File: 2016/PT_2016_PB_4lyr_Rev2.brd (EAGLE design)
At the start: 154.7 x 201.9 mm, 156 parts, among them Q12 2N7002, Q2 2N7002

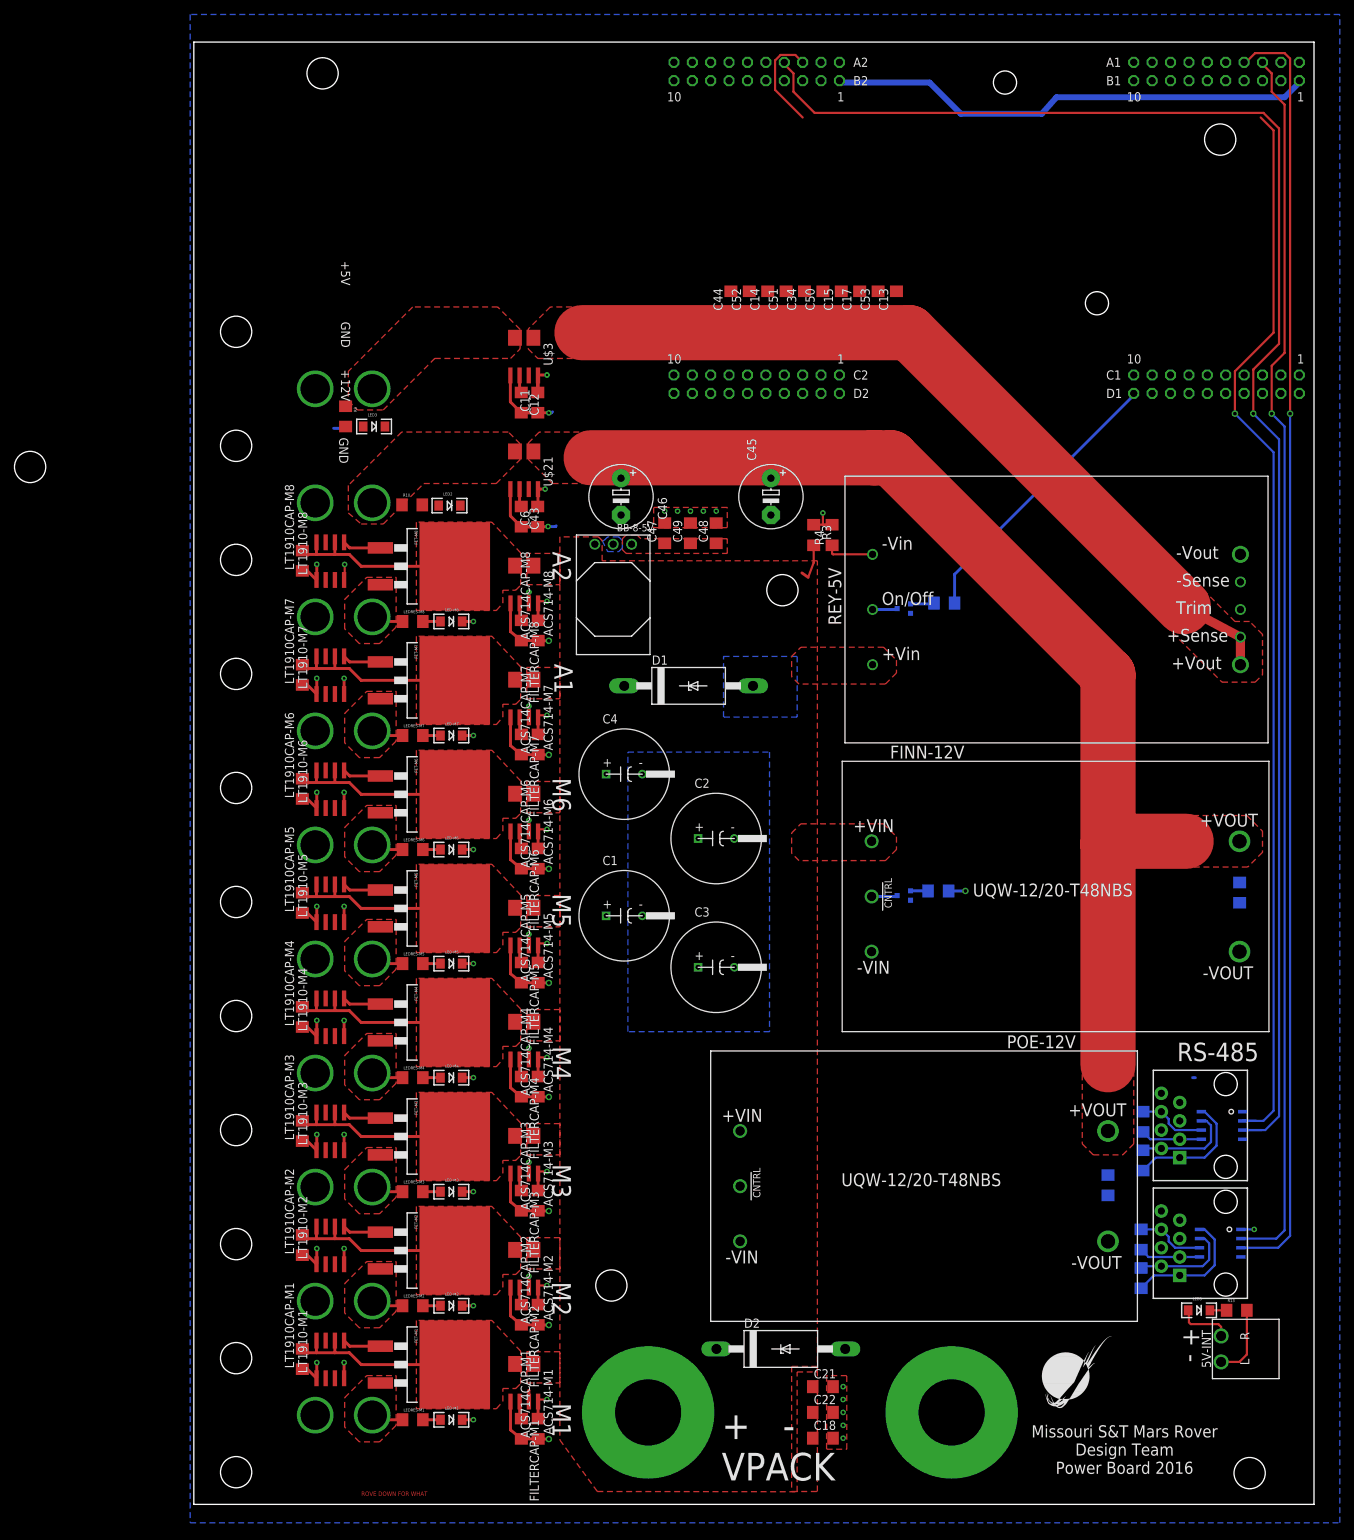
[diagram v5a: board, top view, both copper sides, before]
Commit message: Finished routing 4-layer
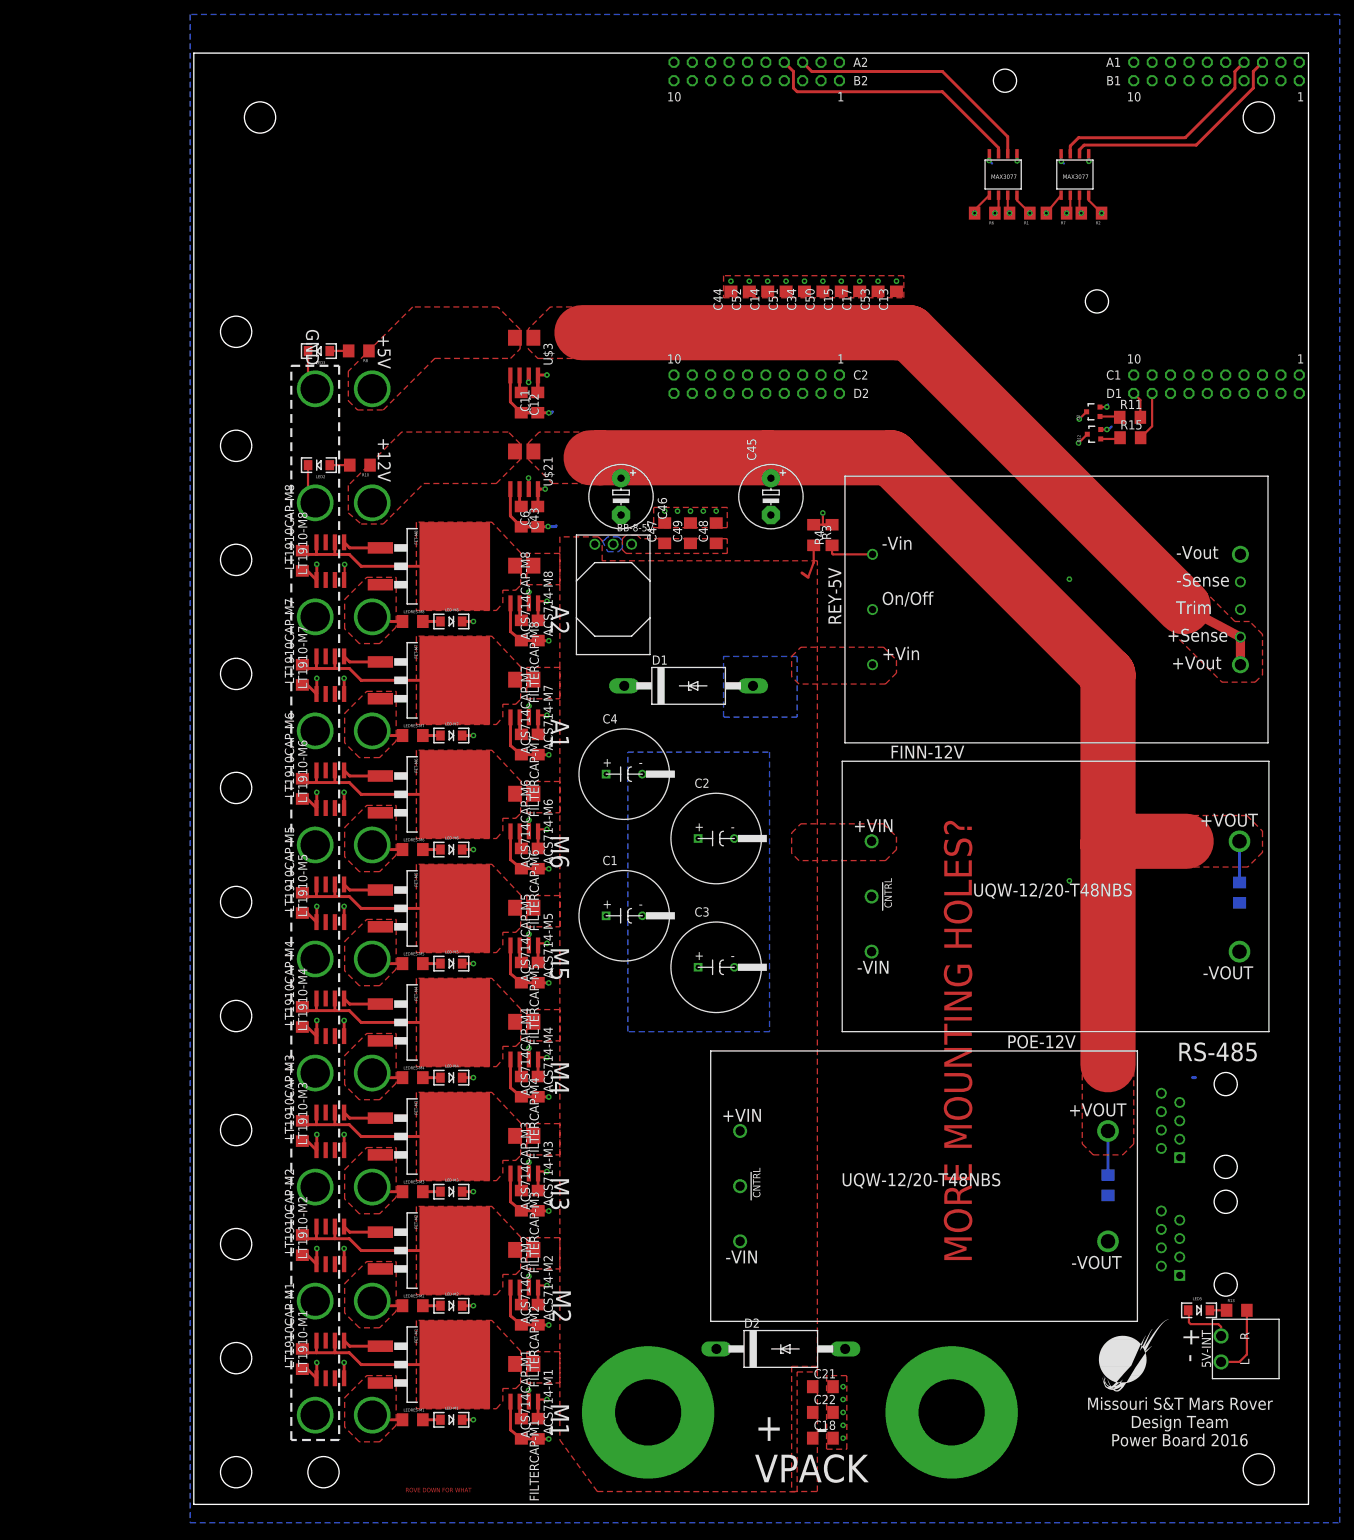
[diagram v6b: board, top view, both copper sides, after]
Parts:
- removed U$23: RJ45-8PTH, SparkFun-Connectors:RJ45-8
- added U$6: RJ45FCI-54602-908LF, MRDT-2015-General:FCI-54602-908LF
- U$5: value RJ45-8PTH -> RJ45FCI-54602-908LF; device SparkFun-Connectors:RJ45-8 -> MRDT-2015-General:FCI-54602-908LF
- moved U$24 148.9 mm to (116.8, 179.8), flipped to the top, turned to 180 degrees
- moved R2 147.2 mm to (119.1, 174.5), flipped to the top, turned to 180 degrees
- moved R7 142.2 mm to (114.3, 174.5), flipped to the top, turned to 180 degrees
- moved U$12 134.8 mm to (106.9, 179.8), flipped to the top, turned to 180 degrees
- moved R1 131.9 mm to (109.2, 174.5), flipped to the top, turned to 180 degrees
- moved R6 127.4 mm to (104.4, 174.5), flipped to the top, turned to 180 degrees
- moved Q12 68.9 mm to (119.5, 144.0), flipped to the top, turned to 90 degrees
- moved R15 68.0 mm to (124.5, 143.5), flipped to the top, turned to 0 degrees
- moved Q2 37.7 mm to (119.4, 147.1), flipped to the top, turned to 90 degrees
- moved R11 36.3 mm to (124.5, 146.3), flipped to the top, turned to 0 degrees
- moved LED2 18.9 mm to (12.4, 139.7), turned to 180 degrees
- moved LED3 12.9 mm to (12.4, 155.4), turned to 180 degrees
- moved R8 9.23 mm to (18.0, 155.5), turned to 180 degrees
- moved R10 9.06 mm to (18.1, 139.7), turned to 180 degrees
- moved U$22 8.20 mm to (120.1, 10.9)
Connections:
- removed net N$108: U$1.PD3
- removed net N$118: U$1.PE5
- net 12V-IMEAS: now also U$1.PD3; no longer U$1.PD1
- net 5V-IMEAS: now also U$1.PE5; no longer U$1.PD0
- net GND: now also U$6.7, U$6.8; no longer U$23.7, U$23.8
- net REC+: now also U$6.1; no longer U$5.1
- net REC+1: now also U$5.1; no longer U$23.1
- net REC-: now also U$6.2; no longer U$5.2
- net REC-1: now also U$5.2; no longer U$23.2
- net TRANS+: now also U$6.3; no longer U$5.3
- net TRANS+1: now also U$5.3; no longer U$23.3
- net TRANS-: now also U$6.6; no longer U$5.6
- net TRANS-1: now also U$5.6; no longer U$23.6
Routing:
- net M1-IMEAS: track 227.9 -> 0.00 mm
- net IMEAS-M2: track 1.56 -> 220.9 mm
- net M2-IMEAS: track 212.1 -> 0.00 mm
- net IMEAS-M3: track 1.56 -> 204.7 mm
- net M4-IMEAS: track 200.1 -> 0.00 mm
- net M3-IMEAS: track 197.0 -> 0.00 mm
- net IMEAS-M4: track 1.56 -> 190.8 mm
- net TX2: track 221.2 -> 36.6 mm, vias 1 -> 0
- net M5-IMEAS: track 179.4 -> 0.00 mm
- net IMEAS-M1: track 60.8 -> 238.8 mm, vias 0 -> 1
- net IMEAS-M5: track 1.56 -> 170.1 mm
- net TRANS+: track 8.48 -> 175.1 mm, vias 0 -> 1
- net 12V-IMEAS: track 0.00 -> 155.4 mm, vias 0 -> 1
- net IMEAS-M6: track 1.56 -> 153.9 mm
- net REC-: track 13.8 -> 165.6 mm, vias 0 -> 1
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- added copper zone on layer 1, net N$71
- removed copper zone on layer 1, net N$72
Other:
- board size 154.7 x 201.9 mm -> 153.9 x 200.4 mm
- board text added: "MORE MOUNTING HOLES?"
